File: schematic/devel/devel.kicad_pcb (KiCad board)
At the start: 2 copper layers, 60 x 59.7 mm, 40 parts, among them J1 CONN_PWR, J2 CONN_X1, J3 CONN_Y2, J4 CONN_X2, J5 CONN_Y1, U1 L7812, U2 L7912, U3 REF5010IDGK, U4 OPA4197

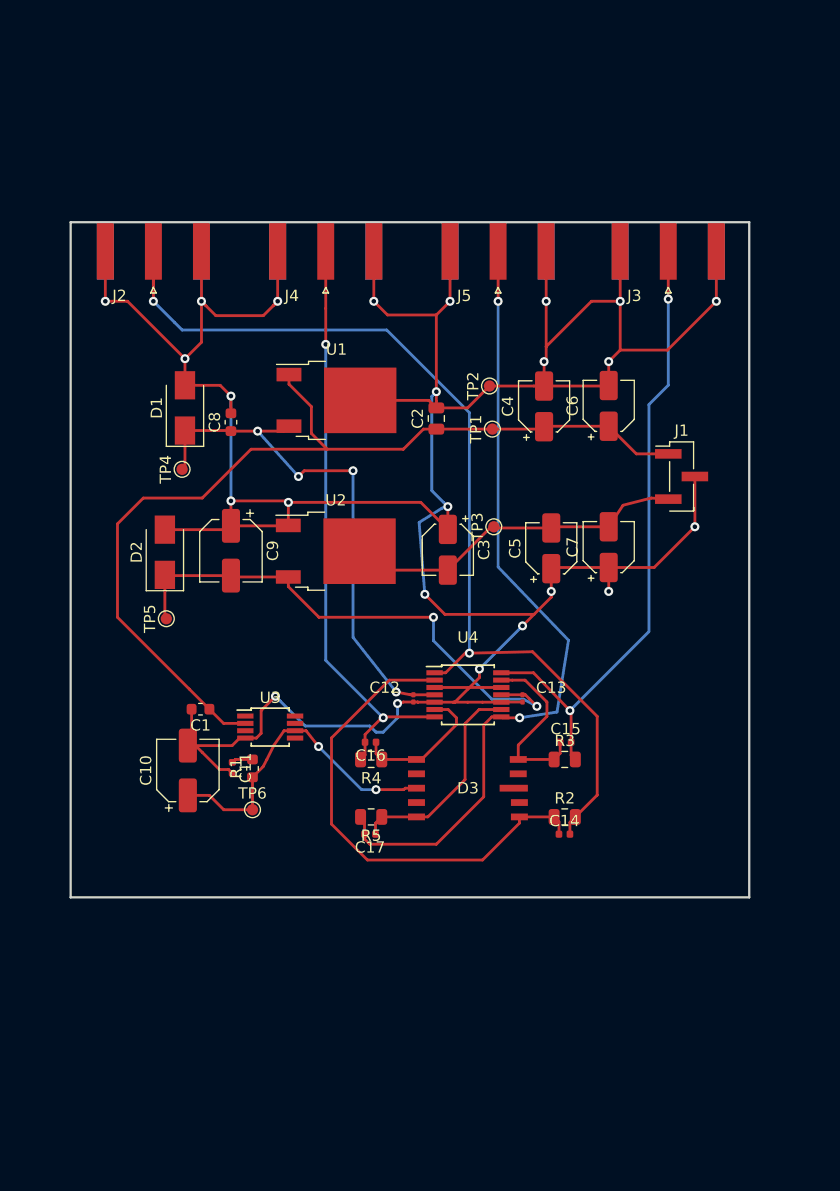
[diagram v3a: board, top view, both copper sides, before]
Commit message: simplified circuit schematic, used uniform resistor footprints
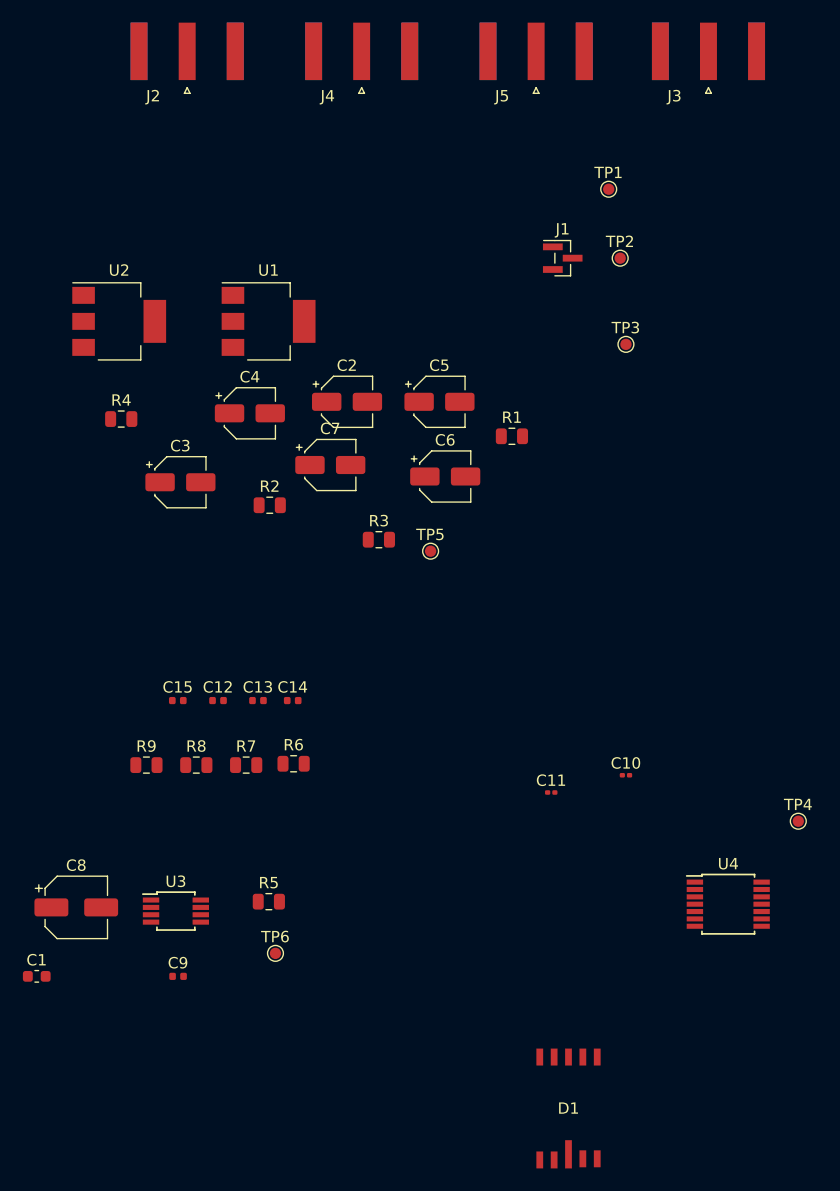
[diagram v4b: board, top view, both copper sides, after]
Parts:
- removed C16, C17: 4p, Capacitor_SMD:C_0402_1005Metric
- removed D2: D_Schottky, Diode_SMD:D_SMA
- removed D3: S599x, Sensor_OpticalPosition:S5990
- added R6: 100k, Resistor_SMD:R_0805_2012Metric, F.Cu at (115.9, 136.1)
- added R7: 100k, Resistor_SMD:R_0805_2012Metric, F.Cu at (111.7, 136.3)
- added R8: 100k, Resistor_SMD:R_0805_2012Metric, F.Cu at (107.3, 136.3)
- added R9: 100k, Resistor_SMD:R_0805_2012Metric, F.Cu at (102.9, 136.3)
- C1: value 330n -> 0.33u
- C10: value 22u -> 0.1u; footprint Capacitor_SMD:CP_Elec_5x5.4 -> Capacitor_SMD:C_0201_0603Metric
- C11: value 10n -> 0.1u; footprint Capacitor_SMD:C_0402_1005Metric -> Capacitor_SMD:C_0201_0603Metric
- C12, C13: value 100n -> 4p; footprint Capacitor_SMD:C_0201_0603Metric -> Capacitor_SMD:C_0402_1005Metric
- C2: value 330n -> 0.1u; footprint Capacitor_SMD:C_0805_2012Metric -> Capacitor_SMD:CP_Elec_4x3.9
- C3: value 2.2u -> 0.1u; footprint Capacitor_SMD:CP_Elec_4x5.4 -> Capacitor_SMD:CP_Elec_4x3.9
- C4, C5, C6, C7: footprint Capacitor_SMD:CP_Elec_4x5.4 -> Capacitor_SMD:CP_Elec_4x3.9
- C8: value 100n -> 22u; footprint Capacitor_SMD:C_0603_1608Metric -> Capacitor_SMD:CP_Elec_5x5.4
- C9: value 1u -> 10n; footprint Capacitor_SMD:CP_Elec_5x4.4 -> Capacitor_SMD:C_0402_1005Metric
- D1: value D_Schottky -> S599x; footprint Diode_SMD:D_SMA -> Sensor_OpticalPosition:S5990
- J1: footprint Connector_PinHeader_2.00mm:PinHeader_1x03_P2.00mm_Vertical_SMD_Pin1Left -> Connector_PinHeader_1.00mm:PinHeader_1x03_P1.00mm_Vertical_SMD_Pin1Left
- R1: value 100 -> 120; footprint Resistor_SMD:R_0603_1608Metric -> Resistor_SMD:R_0805_2012Metric
- R2, R3: value 100k -> 1050
- R4: value 100k -> 120
- R5: value 100k -> 100
- U1: value L7812 -> LM317_SOT223; footprint Package_TO_SOT_SMD:TO-252-2 -> Package_TO_SOT_SMD:SOT-223-3_TabPin2
- U2: value L7912 -> LM337_SOT223; footprint Package_TO_SOT_SMD:TO-252-2 -> Package_TO_SOT_SMD:SOT-223-3_TabPin2
- moved D1 70.6 mm to (140.2, 166.6), turned to 0 degrees
- moved TP4 62.7 mm to (160.5, 141.2), turned to 0 degrees
- moved C8 45.0 mm to (96.7, 148.8), turned to 0 degrees
- moved C10 38.7 mm to (145.3, 137.2), turned to 0 degrees
- moved R2 37.9 mm to (113.8, 113.3)
- moved C9 37.9 mm to (105.7, 154.9), turned to 0 degrees
- moved R4 37.3 mm to (100.7, 105.7), turned to 0 degrees
- moved R1 37.3 mm to (135.2, 107.2), turned to 0 degrees
- moved C15 34.5 mm to (105.7, 130.6)
- moved U4 29.5 mm to (154.3, 148.6)
- moved C11 28.3 mm to (138.7, 138.7), turned to 0 degrees
- moved U2 27.9 mm to (100.5, 97.0)
- moved C1 27.7 mm to (93.2, 154.9), turned to 0 degrees
- moved C14 26.8 mm to (115.8, 130.6)
- moved C4 26.0 mm to (112.0, 105.2), turned to 0 degrees
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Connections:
- C10 pad 1: Net-(C10-Pad1) -> GND
- C10 pad 2: GND -> +12V
- C11 pad 1: Net-(C11-Pad1) -> GND
- C11 pad 2: GND -> -12V
- C12 pad 1: GND -> Net-(C12-Pad1)
- C12 pad 2: +12V -> Net-(C12-Pad2)
- C13 pad 1: GND -> Net-(C13-Pad1)
- C13 pad 2: -12V -> Net-(C13-Pad2)
- C4 pad 1: +15V -> Net-(C4-Pad1)
- C5 pad 2: -15V -> Net-(C5-Pad2)
- C6 pad 1: +15V -> +12V
- C7 pad 2: -15V -> -12V
- C8 pad 1: +12V -> Net-(C8-Pad1)
- C9 pad 1: GND -> Net-(C9-Pad1)
- C9 pad 2: -12V -> GND
- D1 pad 1: +12V -> Net-(C12-Pad1)
- D1 pad 2: GND -> (no net)
- J2 pad 1: Net-(C14-Pad2) -> Net-(C12-Pad2)
- J3 pad 1: Net-(C15-Pad2) -> Net-(C13-Pad2)
- J4 pad 1: Net-(C16-Pad2) -> Net-(C14-Pad2)
- J5 pad 1: Net-(C17-Pad2) -> Net-(C15-Pad2)
- R1 pad 1: Net-(C10-Pad1) -> +12V
- R1 pad 2: Net-(C11-Pad1) -> Net-(C4-Pad1)
- R2 pad 1: Net-(C14-Pad1) -> Net-(C4-Pad1)
- R2 pad 2: Net-(C14-Pad2) -> GND
- R3 pad 1: Net-(C15-Pad1) -> GND
- R3 pad 2: Net-(C15-Pad2) -> Net-(C5-Pad2)
- R4 pad 1: Net-(C16-Pad1) -> Net-(C5-Pad2)
- R4 pad 2: Net-(C16-Pad2) -> -12V
- R5 pad 1: Net-(C17-Pad1) -> Net-(C8-Pad1)
- R5 pad 2: Net-(C17-Pad2) -> Net-(C9-Pad1)
- TP6 pad 1: Net-(C10-Pad1) -> Net-(C8-Pad1)
- U1 pad 1: +15V -> Net-(C4-Pad1)
- U1 pad 2: GND -> +12V
- U1 pad 3: +12V -> +15V
- U2 pad 1: GND -> Net-(C5-Pad2)
- U3 pad 6: Net-(C10-Pad1) -> Net-(C8-Pad1)
- U4 pad 1: Net-(C14-Pad2) -> Net-(C12-Pad2)
- U4 pad 13: Net-(C15-Pad1) -> Net-(C13-Pad1)
- U4 pad 14: Net-(C15-Pad2) -> Net-(C13-Pad2)
- U4 pad 2: Net-(C14-Pad1) -> Net-(C12-Pad1)
- U4 pad 6: Net-(C16-Pad1) -> Net-(C14-Pad1)
- U4 pad 7: Net-(C16-Pad2) -> Net-(C14-Pad2)
- U4 pad 8: Net-(C17-Pad2) -> Net-(C15-Pad2)
- U4 pad 9: Net-(C17-Pad1) -> Net-(C15-Pad1)
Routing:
- net GND: track 302.4 -> 0.00 mm, vias 24 -> 0
- net Net-(C14-Pad2): track 93.2 -> 0.00 mm, vias 2 -> 0
- net +15V: track 84.7 -> 0.00 mm
- net Net-(C17-Pad2): track 71.1 -> 0.00 mm, vias 2 -> 0
- net Net-(C15-Pad2): track 56.3 -> 0.00 mm, vias 2 -> 0
- net Net-(C16-Pad2): track 52.5 -> 0.00 mm, vias 2 -> 0
- net +12V: track 47.7 -> 0.00 mm, vias 4 -> 0
- net -12V: track 46.8 -> 0.00 mm, vias 2 -> 0
- net Net-(C14-Pad1): track 43.5 -> 0.00 mm
- net Net-(C10-Pad1): track 28.4 -> 0.00 mm, vias 2 -> 0
- net -15V: track 27.4 -> 0.00 mm
- net Net-(C17-Pad1): track 19.2 -> 0.00 mm
- net Net-(C15-Pad1): track 15.9 -> 0.00 mm
- net Net-(C16-Pad1): track 12.5 -> 0.00 mm
- net Net-(C11-Pad1): track 1.88 -> 0.00 mm
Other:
- board outline removed

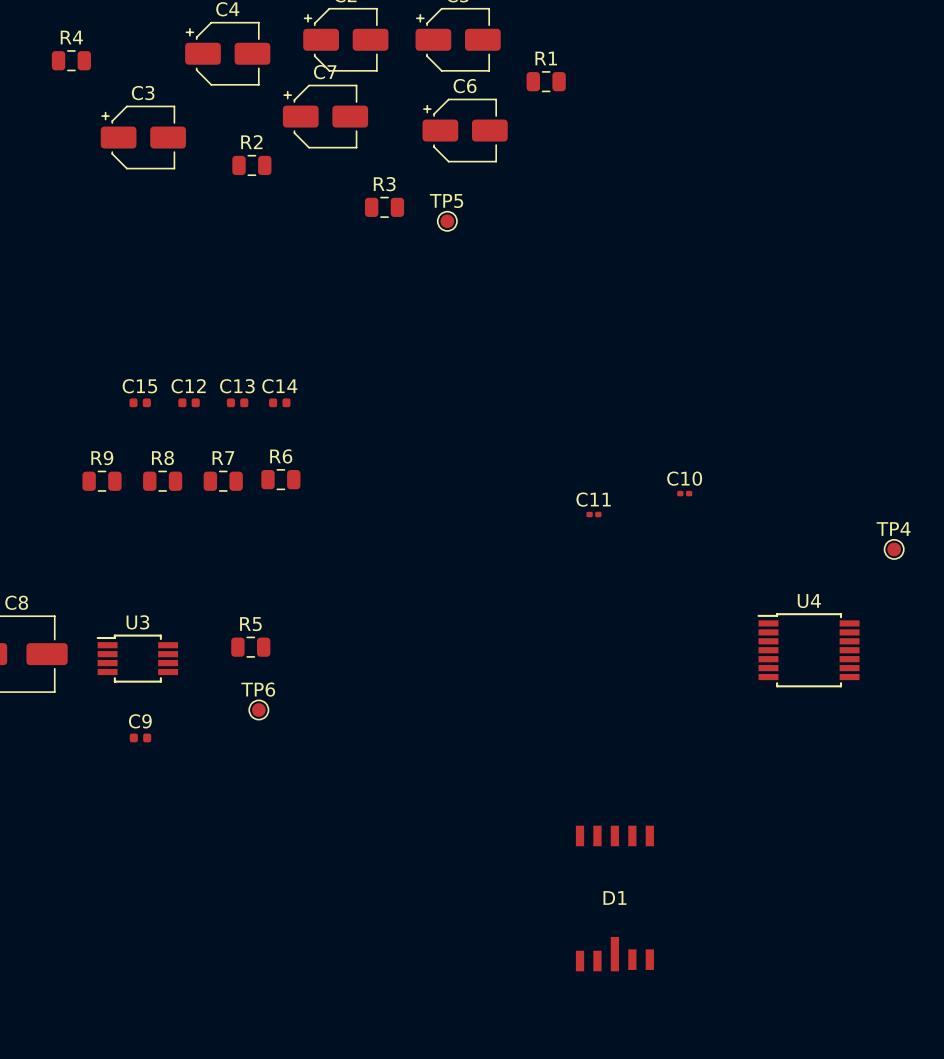
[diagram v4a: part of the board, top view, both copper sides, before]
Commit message: completed sublayout of detector and preamp
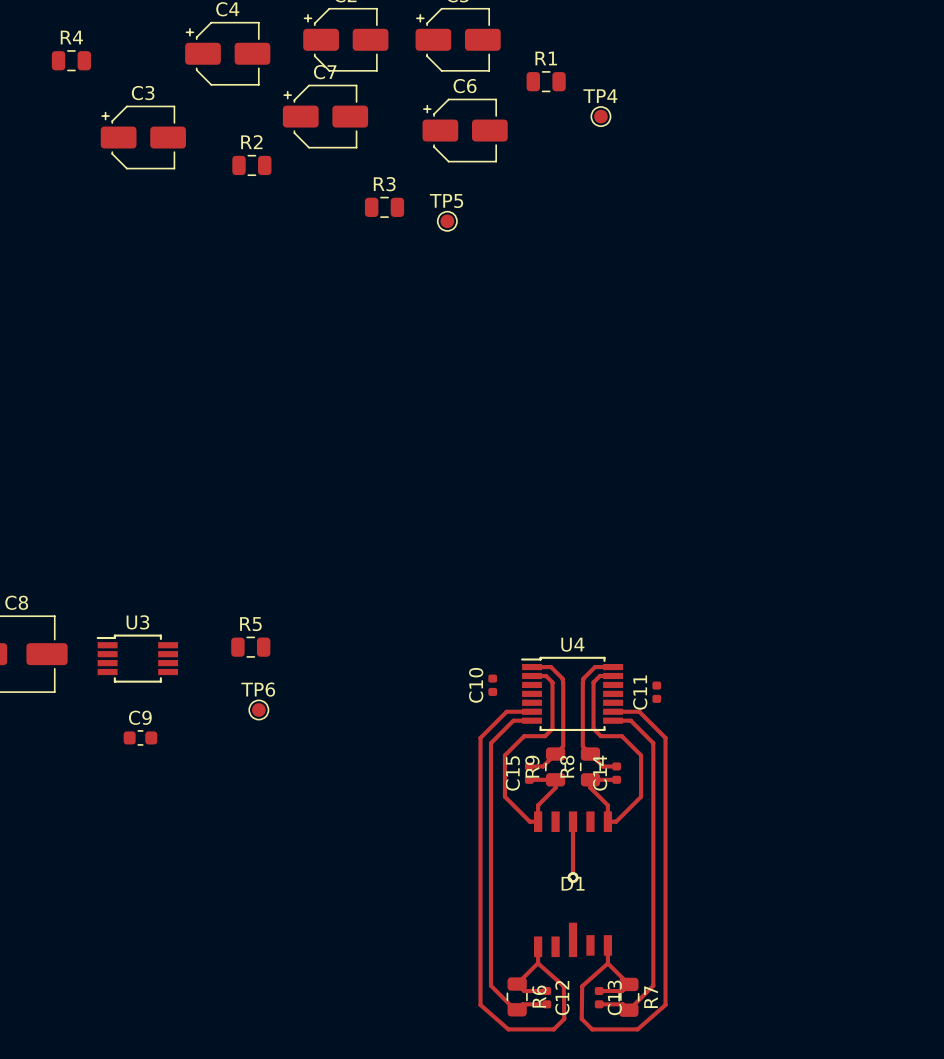
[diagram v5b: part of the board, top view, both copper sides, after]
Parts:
- C10, C11: footprint Capacitor_SMD:C_0201_0603Metric -> Capacitor_SMD:C_0402_1005Metric
- C9: footprint Capacitor_SMD:C_0402_1005Metric -> Capacitor_SMD:C_0603_1608Metric
- moved C13 50.7 mm to (139.1, 173.8), turned to 270 degrees
- moved C12 50.5 mm to (135.3, 173.8), turned to 270 degrees
- moved R7 47.8 mm to (141.2, 173.8), turned to 270 degrees
- moved R6 41.4 mm to (133.1, 173.8), turned to 270 degrees
- moved C15 39.1 mm to (134.0, 157.5), turned to 90 degrees
- moved R9 39.0 mm to (135.9, 157.1), turned to 90 degrees
- moved TP4 38.0 mm to (139.2, 109.7)
- moved R8 37.4 mm to (138.4, 157.1), turned to 90 degrees
- moved C14 36.4 mm to (140.3, 157.5), turned to 90 degrees
- moved C10 19.7 mm to (131.3, 151.1), turned to 90 degrees
- moved U4 17.5 mm to (137.1, 151.7)
- moved C11 13.7 mm to (143.3, 151.6), turned to 90 degrees
- moved D1 3.22 mm to (137.2, 165.6)
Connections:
- U4 pad 1: Net-(C12-Pad2) -> Net-(C15-Pad2)
- U4 pad 13: Net-(C13-Pad1) -> Net-(C14-Pad1)
- U4 pad 14: Net-(C13-Pad2) -> Net-(C14-Pad2)
- U4 pad 2: Net-(C12-Pad1) -> Net-(C15-Pad1)
- U4 pad 6: Net-(C14-Pad1) -> Net-(C12-Pad1)
- U4 pad 7: Net-(C14-Pad2) -> Net-(C12-Pad2)
- U4 pad 8: Net-(C15-Pad2) -> Net-(C13-Pad2)
- U4 pad 9: Net-(C15-Pad1) -> Net-(C13-Pad1)
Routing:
- net Net-(C13-Pad1): track 0.00 -> 41.8 mm
- net Net-(C12-Pad1): track 0.00 -> 41.7 mm
- net Net-(C13-Pad2): track 0.00 -> 26.1 mm
- net Net-(C12-Pad2): track 0.00 -> 26.1 mm
- net Net-(C14-Pad1): track 0.00 -> 21.0 mm
- net Net-(C15-Pad1): track 0.00 -> 21.0 mm
- net Net-(C14-Pad2): track 0.00 -> 10.6 mm
- net Net-(C15-Pad2): track 0.00 -> 10.6 mm
- net Net-(C8-Pad1): track 0.00 -> 4.06 mm, vias 0 -> 1
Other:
- net class Default: clearance 0.2 -> 0.1
- rule trace_clearance: 0.2 -> 0.1
- rule trace_min: 0.2 -> 0.15

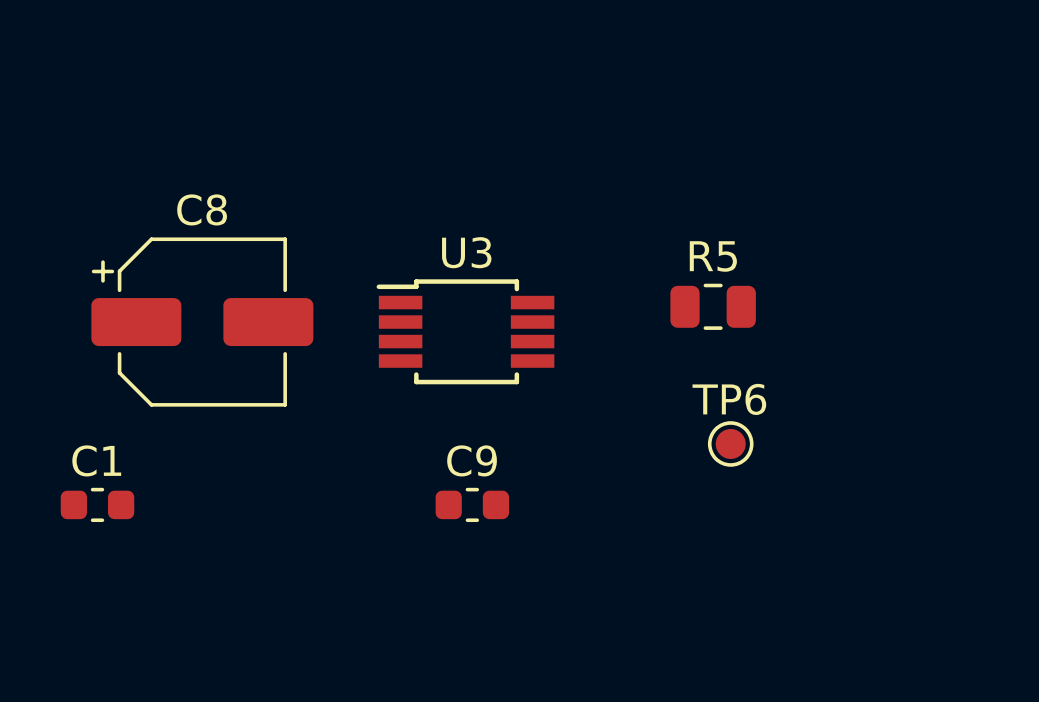
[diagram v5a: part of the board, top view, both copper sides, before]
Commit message: completed sublayout of bias voltage reference
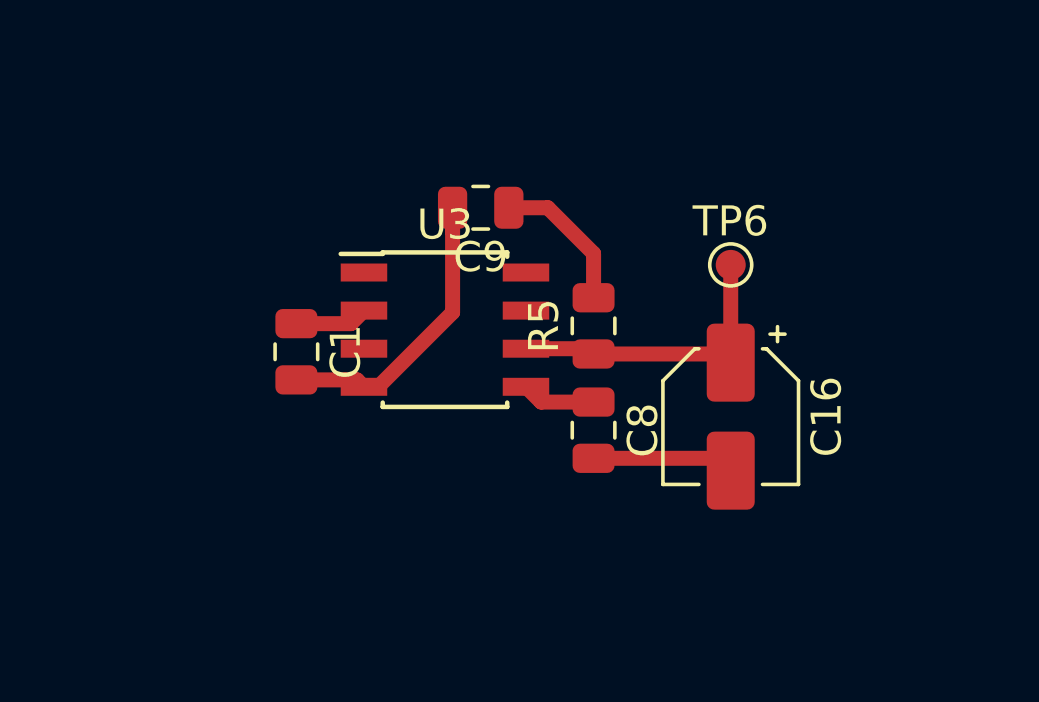
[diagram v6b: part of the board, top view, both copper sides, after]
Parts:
- added C16: 22u, Capacitor_SMD:CP_Elec_4x3.9, F.Cu at (114.3, 152.0)
- C1: value 0.33u -> 1u; footprint Capacitor_SMD:C_0603_1608Metric -> Capacitor_SMD:C_0805_2012Metric
- C8: value 22u -> 1u; footprint Capacitor_SMD:CP_Elec_5x5.4 -> Capacitor_SMD:C_0805_2012Metric
- C9: footprint Capacitor_SMD:C_0603_1608Metric -> Capacitor_SMD:C_0805_2012Metric
- U3: footprint Package_SO:MSOP-8_3x3mm_P0.65mm -> Package_SO:SOIC-8_3.9x4.9mm_P1.27mm
- moved C8 13.5 mm to (109.7, 152.4), turned to 270 degrees
- moved C9 9.91 mm to (106.0, 145.0), turned to 180 degrees
- moved C1 8.37 mm to (99.8, 149.8), turned to 270 degrees
- moved TP6 5.97 mm to (114.3, 146.9)
- moved R5 4.04 mm to (109.7, 149.0), turned to 90 degrees
- moved U3 0.72 mm to (104.8, 149.1)
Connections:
- D1 pad 8: Net-(C8-Pad1) -> Net-(C16-Pad1)
- R5 pad 1: Net-(C8-Pad1) -> Net-(C16-Pad1)
- TP6 pad 1: Net-(C8-Pad1) -> Net-(C16-Pad1)
- U3 pad 5: Net-(U3-Pad5) -> Net-(C8-Pad1)
- U3 pad 6: Net-(C8-Pad1) -> Net-(C16-Pad1)
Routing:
- net GND: track 0.00 -> 14.6 mm
- net Net-(C16-Pad1): track 0.00 -> 14.3 mm, vias 0 -> 1
- net Net-(C9-Pad1): track 0.00 -> 4.93 mm
- net +15V: track 0.00 -> 2.43 mm
- net Net-(C8-Pad1): track 4.06 -> 2.46 mm, vias 1 -> 0
